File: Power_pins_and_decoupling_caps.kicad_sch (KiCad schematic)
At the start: 87 parts, among them U1 74LS30, U10 74LS13, U11 74LS10, U12 74LS393, U15 74LS20, U16 74LS04, U17 74LS55, U18 74LS55, U19 74LS393, U2 74LS04, U20 74LS158, U21 MM5280, U22 MM5280, U23 MM5280, U24 MM5280, U25 MM5280, U26 MM5280, U27 MM5280, U28 MM5280, U29 74LS00, U3 74LS10, U30 74LS109, U31 74LS08, U32 74LS393, U33 74LS158, U34 74LS93, U35 74LS158, U36 MM5280, U37 MM5280, U38 MM5280, U39 MM5280, U40 MM5280, U41 MM5280, U42 MM5280, U43 MM5280, U44 74LS26, U45 74LS109, U46 74LS04, U47 74LS20, U5 74LS173, U7 74LS173, U8 74LS368, U9 74LS166

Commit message: Various corrections. Add new symbols and footprints
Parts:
- C11, C12, C13, C34, C35: footprint (none) -> K-1008:C_Disc_D8.0mm_W2.5mm_P6.35mm
- C35: footprint (none) -> K-1008:C_Disc_D8.0mm_W2.5mm_P6.98mm
- U1, U11, U12, U16, U19, U2, U29, U3, U31, U32, U34, U44, U46: footprint (none) -> K-1008:DIP-14_W7.62mm_LongPads
- U10: footprint (none) -> K-1008:DIP-14_W7.62mm_LongPads; symbol 74xx:74LS13 -> K-1008_Library:74LS13
- U15: footprint (none) -> K-1008:DIP-14_W7.62mm_LongPads; symbol K-1008_Library:74LS20_U15 -> K-1008_Library:74LS20
- U17, U18: footprint (none) -> K-1008:DIP-14_W7.62mm_LongPads; symbol 74xx:74LS55 -> K-1008_Library:74LS55
- U20, U30, U33, U35, U45, U5, U7, U8, U9: footprint (none) -> K-1008:DIP-16_W7.62mm_LongPads
- U21, U22, U23, U24, U25, U26, U27, U28, U36, U37, U38, U39, U40, U41, U42, U43: footprint (none) -> K-1008:DIP-22_W10.16mm_LongPads
- U47: footprint (none) -> K-1008:DIP-14_W7.62mm_LongPads; symbol 74xx:74LS20 -> K-1008_Library:74LS20

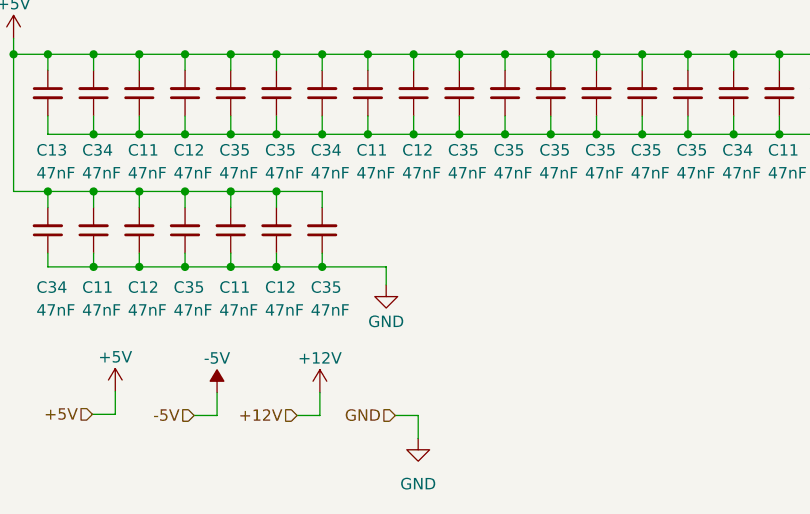
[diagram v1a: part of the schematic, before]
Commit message: C52-C54 connected to -5V, not +5V
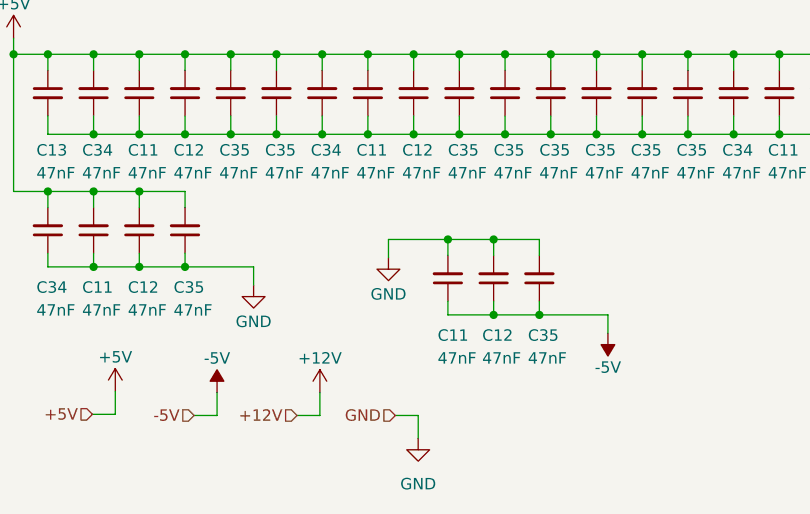
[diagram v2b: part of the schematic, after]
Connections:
- net +5V: no longer C11.2, C12.2, C35.2
- net -5V: now also C11.1, C12.1, C35.1
- net GND: now also C11.2, C12.2, C35.2; no longer C11.1, C12.1, C35.1

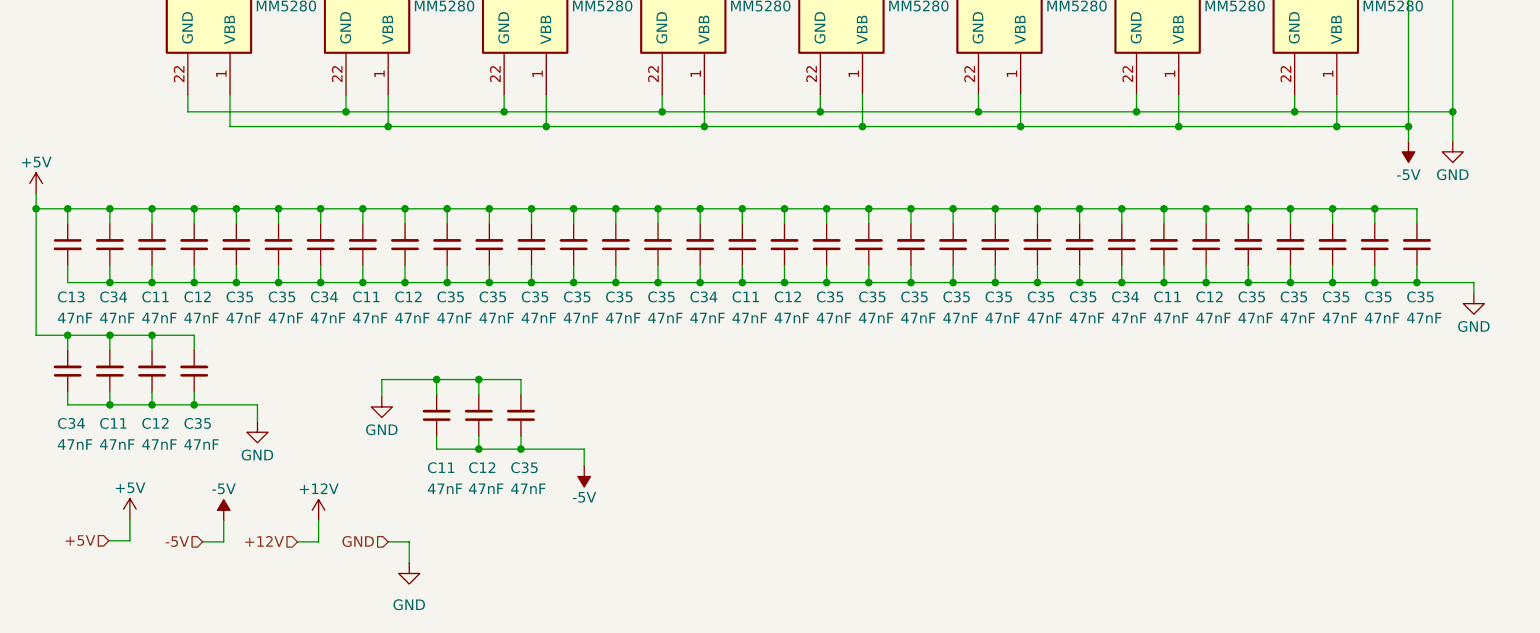
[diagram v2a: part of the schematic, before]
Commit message: C36 to C43 connect to +12V
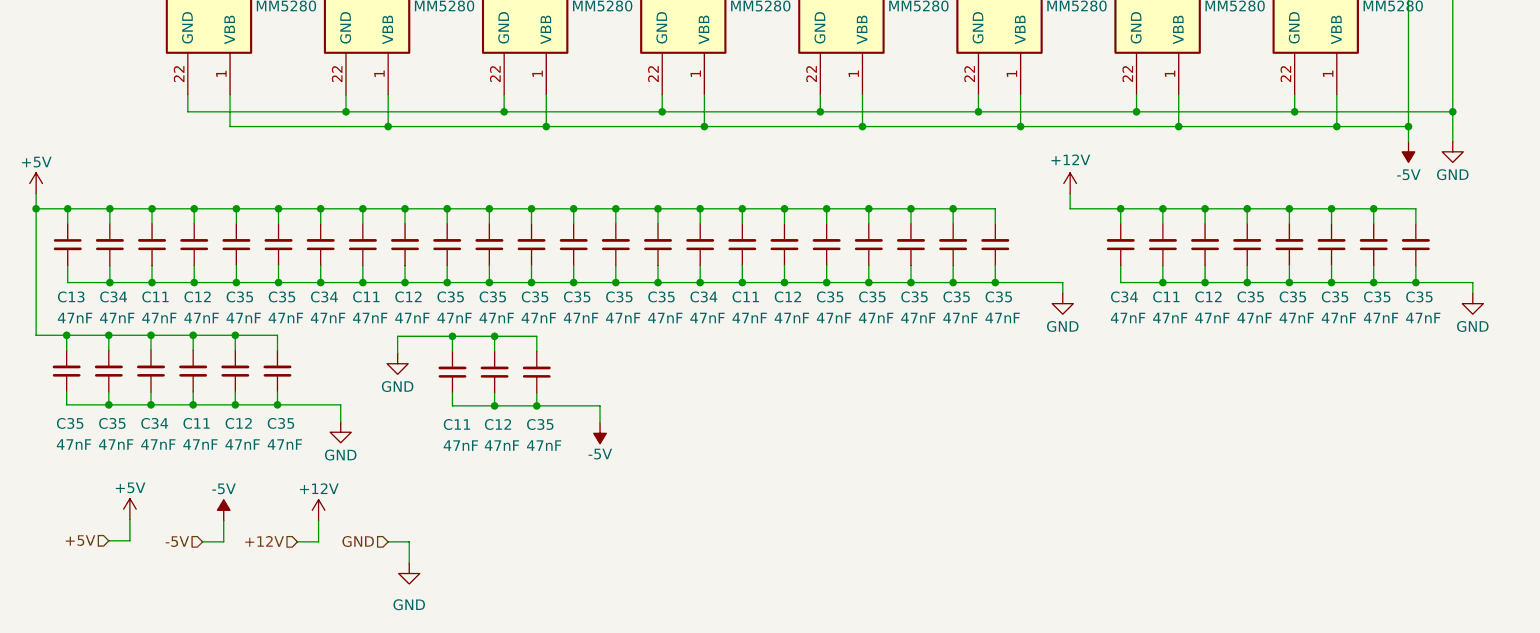
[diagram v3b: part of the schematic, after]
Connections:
- net +12V: now also C11.2, C12.2, C34.2, C35.2, C35.2, C35.2, C35.2, C35.2
- net +5V: no longer C11.2, C12.2, C34.2, C35.2, C35.2, C35.2, C35.2, C35.2
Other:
- moved on the sheet: C11, C12, C34, C35

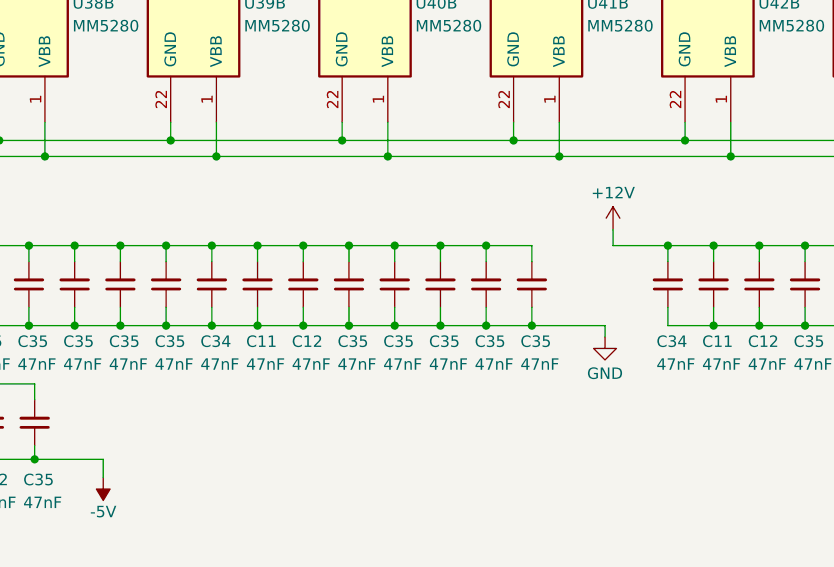
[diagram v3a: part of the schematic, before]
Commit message: C23 to C30 connect to +12V
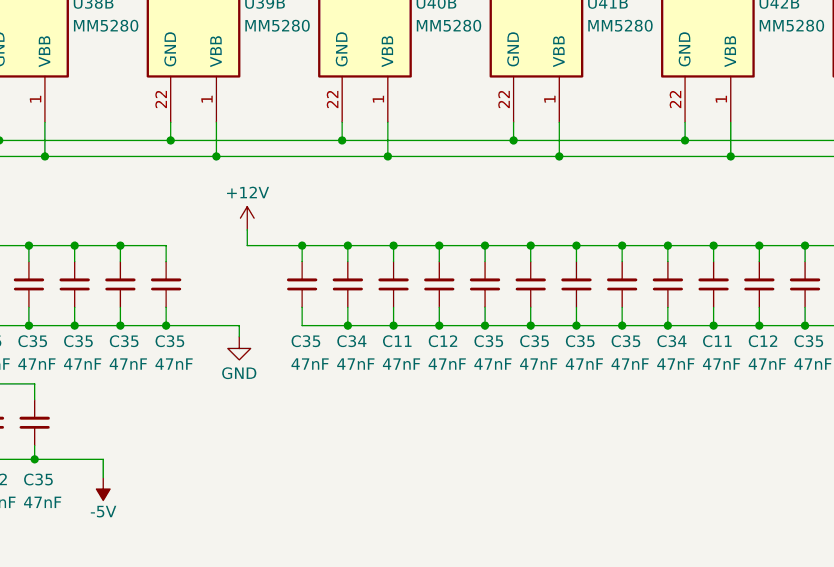
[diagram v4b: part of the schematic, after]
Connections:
- net +12V: now also C11.2, C12.2, C34.2, C35.2, C35.2, C35.2, C35.2, C35.2
- net +5V: no longer C11.2, C12.2, C34.2, C35.2, C35.2, C35.2, C35.2, C35.2
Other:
- moved on the sheet: C11, C12, C34, C35

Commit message: Routing completed
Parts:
- removed U1: 74LS30, K-1008:DIP-14_W7.62mm_LongPads, symbol 74xx:74LS30
- added U1: 74LS30, K-1008:DIP-14_W7.62mm_LongPads, symbol K-1008_Library:74LS30
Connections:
- net +5V: now also U1.14 (VCC)
- net GND: now also U1.7 (GND)
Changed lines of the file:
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@@
     (pin "1")
     (pin "2")
-    (pin "3")
-    (pin "4")
-    (pin "5")
-    (pin "6")
-    (pin "10")
-    (pin "11")
-    (pin "12")
-    (pin "13")
-    (pin "8")
-    (pin "9")
-    (pin "14")
-    (pin "7")
+    (pin "4")
+    (pin "5")
+    (pin "6")
+    (pin "10")
+    (pin "12")
+    (pin "13")
+    (pin "8")
+    (pin "9")
+    (pin "14")
+    (pin "7")
+    (pin "11")
+    (pin "3")
     (instances
       (project "k-1008-visable-memory"
@@
     (pin "1")
     (pin "2")
-    (pin "3")
-    (pin "4")
-    (pin "5")
-    (pin "6")
-    (pin "10")
-    (pin "11")
-    (pin "12")
-    (pin "13")
-    (pin "8")
-    (pin "9")
-    (pin "14")
-    (pin "7")
+    (pin "4")
+    (pin "5")
+    (pin "6")
+    (pin "10")
+    (pin "12")
+    (pin "13")
+    (pin "8")
+    (pin "9")
+    (pin "14")
+    (pin "7")
+    (pin "11")
+    (pin "3")
     (instances
       (project "k-1008-visable-memory"
@@
     (pin "3")
     (pin "4")
-    (pin "5")
-    (pin "6")
-    (pin "8")
-    (pin "9")
-    (pin "14")
-    (pin "7")
+    (pin "8")
+    (pin "14")
+    (pin "7")
+    (pin "5")
+    (pin "6")
+    (pin "9")
     (instances
       (project "k-1008-visable-memory"
@@
         (path "/26b75be2-cc06-4542-b320-e8a79c59fd43/0906c6cf-2849-4b98-a9b6-1dd5ceac5d52"
           (reference "#PWR01017") (unit 1)
+        )
+      )
+    )
+  )
+  (symbol (lib_id "K-1008_Library:74LS30") (at 24.638 36.322 0) (unit 2)
+    (in_bom yes) (on_board yes) (dnp no) (fields_autoplaced)
+    (property "Reference" "U1" (at 30.48 35.052 0)
+      (effects (font (size 1.27 1.27)) (justify left))
+    )
+    (property "Value" "74LS30" (at 30.48 37.592 0)
+      (effects (font (size 1.27 1.27)) (justify left))
+    )
+    (property "Footprint" "K-1008:DIP-14_W7.62mm_LongPads" (at 23.114 36.322 0)
+      (effects (font (size 1.27 1.27)) hide)
+    )
+    (property "Datasheet" "http://www.ti.com/lit/gpn/sn74LS30" (at 24.638 36.322 0)
+      (effects (font (size 1.27 1.27)) hide)
+    )
+    (pin "1")
+    (pin "11")
+    (pin "12")
+    (pin "2")
+    (pin "3")
+    (pin "4")
+    (pin "5")
+    (pin "6")
+    (pin "8")
+    (pin "14")
+    (pin "7")
+    (pin "10")
+    (pin "13")
+    (pin "9")
+    (instances
+      (project "k-1008-visable-memory"
+        (path "/26b75be2-cc06-4542-b320-e8a79c59fd43/0906c6cf-2849-4b98-a9b6-1dd5ceac5d52"
+          (reference "U1") (unit 2)
         )
       )
@@
     (pin "1")
     (pin "2")
-    (pin "3")
-    (pin "4")
-    (pin "5")
-    (pin "6")
-    (pin "10")
-    (pin "11")
-    (pin "12")
-    (pin "13")
-    (pin "8")
-    (pin "9")
-    (pin "14")
-    (pin "7")
+    (pin "4")
+    (pin "5")
+    (pin "6")
+    (pin "10")
+    (pin "12")
+    (pin "13")
+    (pin "8")
+    (pin "9")
+    (pin "14")
+    (pin "7")
+    (pin "11")
+    (pin "3")
     (instances
       (project "k-1008-visable-memory"
@@
     (pin "3")
     (pin "4")
-    (pin "5")
-    (pin "6")
-    (pin "8")
-    (pin "9")
-    (pin "14")
-    (pin "7")
+    (pin "8")
+    (pin "14")
+    (pin "7")
+    (pin "5")
+    (pin "6")
+    (pin "9")
     (instances
       (project "k-1008-visable-memory"
@@
         )
       )
-    )
-  )
-  (symbol (lib_id "74xx:74LS30") (at 24.638 36.322 0) (unit 2)
-    (in_bom yes) (on_board yes) (dnp no) (fields_autoplaced)
-    (property "Reference" "U1" (at 31.623 35.687 0)
-      (effects (font (size 1.27 1.27)) (justify left))
-    )
-    (property "Value" "74LS30" (at 31.623 38.227 0)
-      (effects (font (size 1.27 1.27)) (justify left))
-    )
-    (property "Footprint" "K-1008:DIP-14_W7.62mm_LongPads" (at 24.638 36.322 0)
-      (effects (font (size 1.27 1.27)) hide)
-    )
-    (property "Datasheet" "http://www.ti.com/lit/gpn/sn74LS30" (at 24.638 36.322 0)
-      (effects (font (size 1.27 1.27)) hide)
-    )
-    (pin "1")
-    (pin "11")
-    (pin "12")
-    (pin "2")
-    (pin "3")
-    (pin "4")
-    (pin "5")
-    (pin "6")
-    (pin "8")
-    (pin "14")
-    (pin "7")
-    (instances
-      (project "k-1008-visable-memory"
-        (path "/26b75be2-cc06-4542-b320-e8a79c59fd43"
-          (reference "U1") (unit 2)
-        )
-        (path "/26b75be2-cc06-4542-b320-e8a79c59fd43/4efa16a7-9de7-4861-96ca-6a92d894ba65"
-          (reference "U8") (unit 2)
-        )
-        (path "/26b75be2-cc06-4542-b320-e8a79c59fd43/0906c6cf-2849-4b98-a9b6-1dd5ceac5d52"
-          (reference "U1") (unit 2)
-        )
-      )

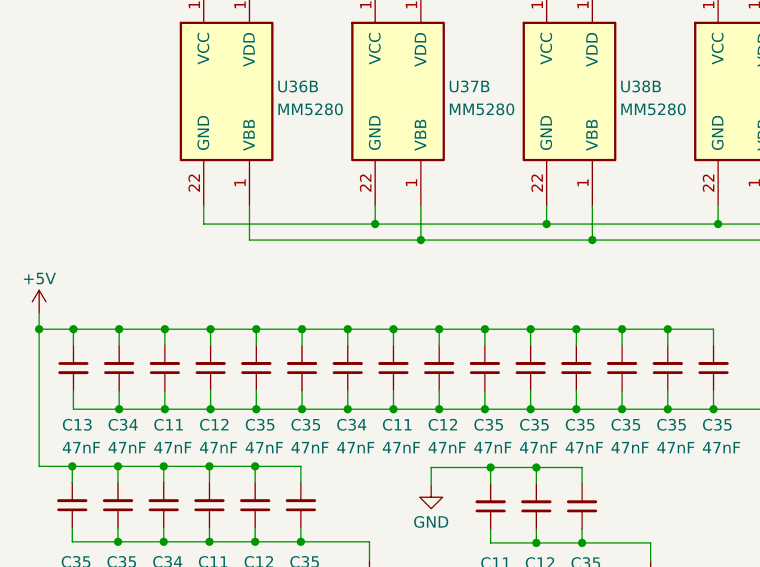
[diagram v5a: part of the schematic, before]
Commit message: Add notes for obsolete parts and replacements
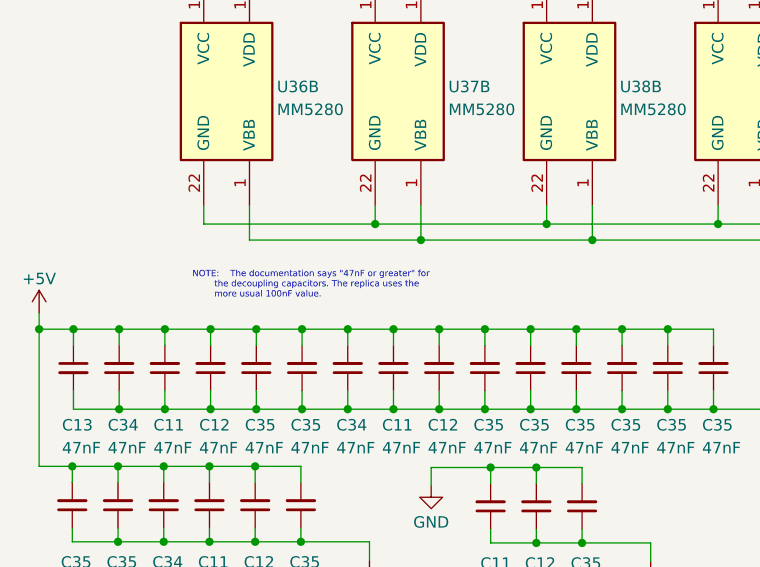
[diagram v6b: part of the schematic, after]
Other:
- note added: "NOTE: The documentation says "47nF or greater" for the decoupling capacitors. The replica uses the more usual 100nF value."
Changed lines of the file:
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@@
     (stroke (width 0) (type default))
+  )
+  (text "NOTE:	The documentation says \"47nF or greater\" for\n		the decoupling capacitors. The replica uses the\n		more usual 100nF value."
+    (at 33.02 231.14 0)
+    (effects (font (size 0.7 0.7) (color 194 0 0 1)) (justify left bottom))
   )
   (hierarchical_label "-5V" (shape input) (at 36.068 274.574 180) (fields_autoplaced)
